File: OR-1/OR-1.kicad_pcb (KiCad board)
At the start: 2 copper layers, 23 x 39.7 mm, 7 parts

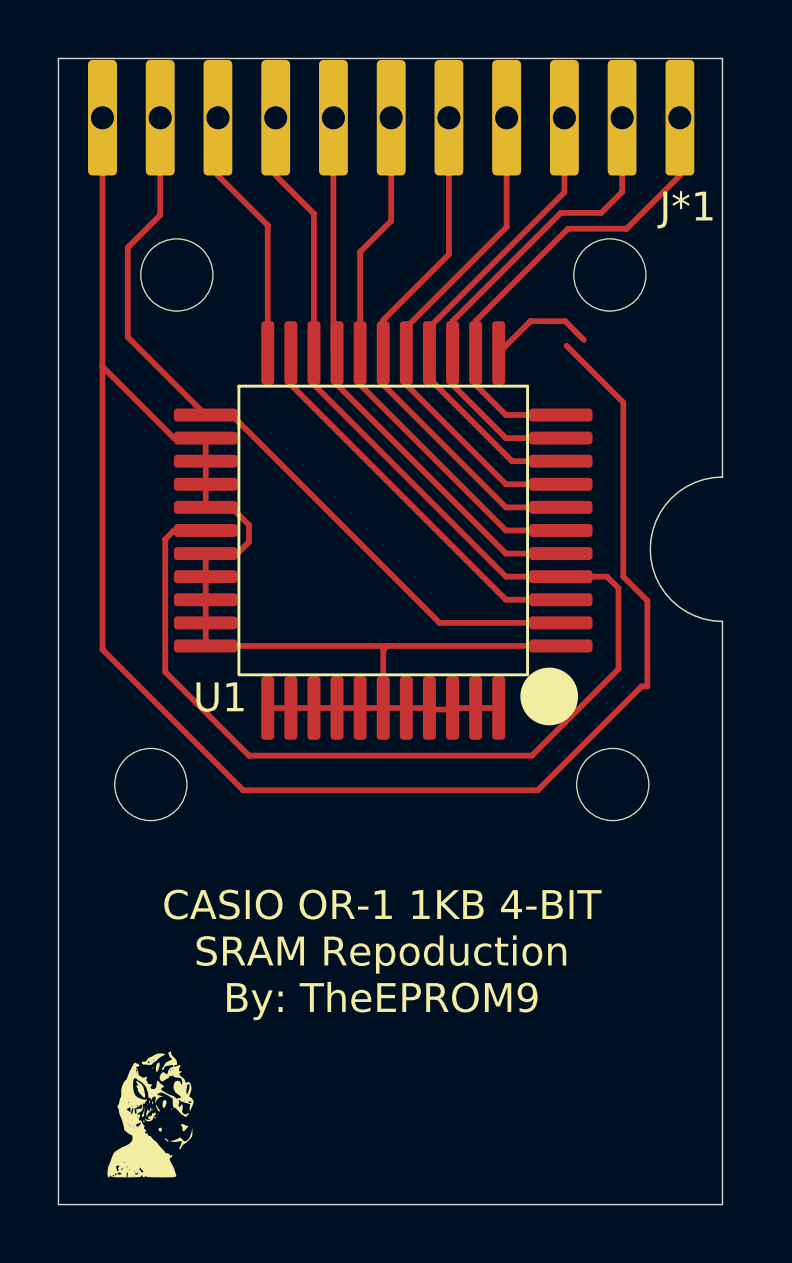
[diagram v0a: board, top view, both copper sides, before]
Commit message: Updated Hole Spacing
Bottom holes were incorrect, ironic really.
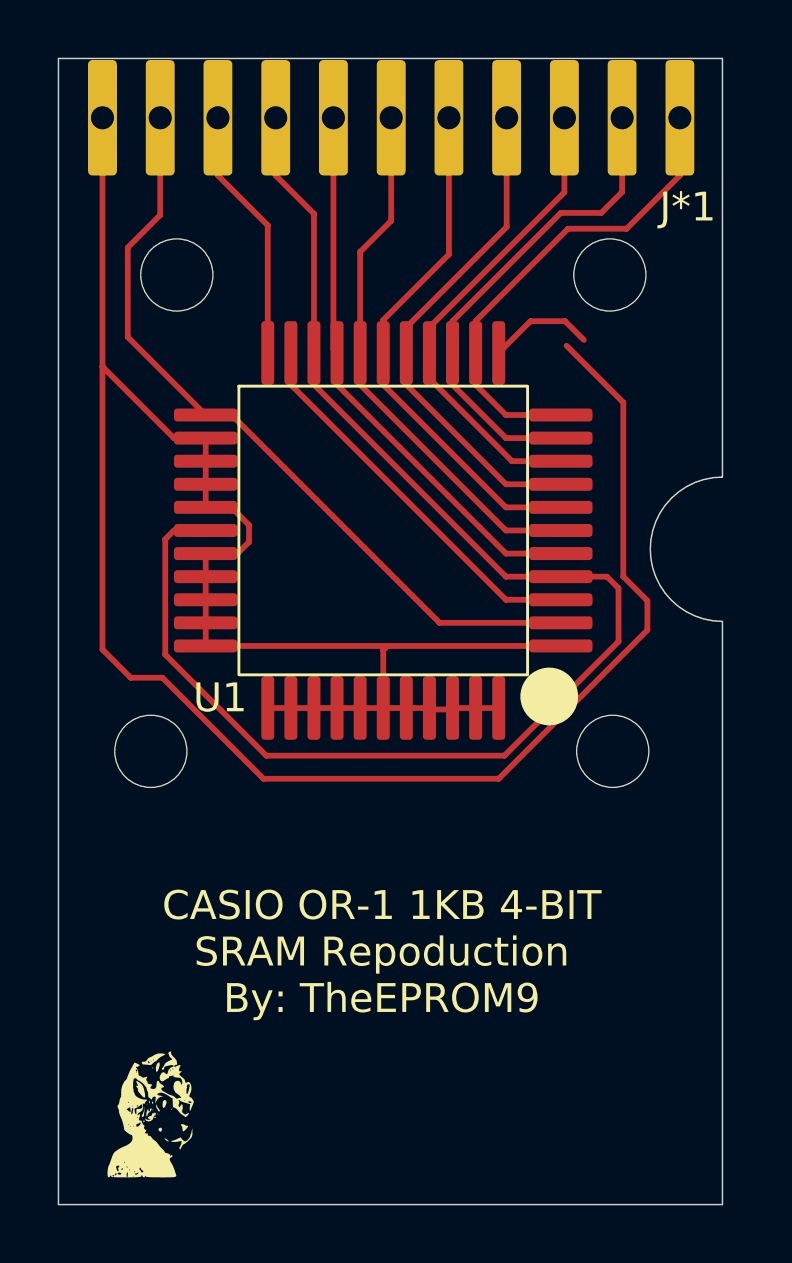
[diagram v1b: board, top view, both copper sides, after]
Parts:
- moved ? 1.15 mm to (141.6, 87.2)
- moved ? 1.15 mm to (157.6, 87.2)
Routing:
- net Net-(J*1-INT/GND): track 89.7 -> 88.2 mm
- net Net-(J*1-VDD2): track 50.3 -> 49.4 mm
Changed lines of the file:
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@@
 	(footprint ""
 		(layer "F.Cu")
-		(at 141.6 88.4)
+		(at 141.6 87.25)
 		(property "Reference" ""
 			(at 0 0 0)
@@
 	(footprint ""
 		(layer "F.Cu")
-		(at 157.6 88.4)
+		(at 157.6 87.25)
 		(property "Reference" ""
 			(at 0 0 0)
@@
 	)
 	(segment
+		(start 142.400001 79.6)
+		(end 142.099 79.901001)
+		(width 0.2)
+		(layer "F.Cu")
+		(net 2)
+	)
+	(segment
 		(start 147.25 74.549999)
 		(end 153.900001 81.2)
@@
 	)
 	(segment
-		(start 142.400001 79.6)
-		(end 142.099 79.901001)
-		(width 0.2)
-		(layer "F.Cu")
-		(net 2)
-	)
-	(segment
-		(start 154.8 87.4)
-		(end 157.8 84.4)
-		(width 0.2)
-		(layer "F.Cu")
-		(net 2)
-	)
-	(segment
-		(start 145 87.4)
-		(end 154.8 87.4)
+		(start 157.8 83.45)
+		(end 157.8 81.6)
 		(width 0.2)
 		(layer "F.Cu")
@@
 	)
 	(segment
+		(start 142.099 79.901001)
+		(end 142.099 83.899)
+		(width 0.2)
+		(layer "F.Cu")
+		(net 2)
+	)
+	(segment
+		(start 153.85 87.4)
+		(end 157.8 83.45)
+		(width 0.2)
+		(layer "F.Cu")
+		(net 2)
+	)
+	(segment
+		(start 145.6 87.4)
+		(end 153.85 87.4)
+		(width 0.2)
+		(layer "F.Cu")
+		(net 2)
+	)
+	(segment
+		(start 142.099 83.899)
+		(end 145.6 87.4)
+		(width 0.2)
+		(layer "F.Cu")
+		(net 2)
+	)
+	(segment
+		(start 147.25 68.629999)
+		(end 147.25 73.45)
+		(width 0.2)
+		(layer "F.Cu")
+		(net 2)
+	)
+	(segment
+		(start 147.25 73.45)
+		(end 147.25 74.549999)
+		(width 0.2)
+		(layer "F.Cu")
+		(net 2)
+	)
+	(segment
+		(start 153.900001 81.2)
+		(end 155.8 81.2)
+		(width 0.2)
+		(layer "F.Cu")
+		(net 2)
+	)
+	(segment
 		(start 157.4 81.2)
 		(end 155.8 81.2)
@@
 	)
 	(segment
-		(start 142.099 84.499)
-		(end 145 87.4)
-		(width 0.2)
-		(layer "F.Cu")
-		(net 2)
-	)
-	(segment
 		(start 143.5 79.6)
 		(end 142.400001 79.6)
@@
 	)
 	(segment
-		(start 142.099 79.901001)
-		(end 142.099 84.499)
-		(width 0.2)
-		(layer "F.Cu")
-		(net 2)
-	)
-	(segment
-		(start 157.8 84.4)
-		(end 157.8 81.6)
-		(width 0.2)
-		(layer "F.Cu")
-		(net 2)
-	)
-	(segment
-		(start 147.25 68.629999)
-		(end 147.25 73.45)
-		(width 0.2)
-		(layer "F.Cu")
-		(net 2)
-	)
-	(segment
-		(start 147.25 73.45)
-		(end 147.25 74.549999)
-		(width 0.2)
-		(layer "F.Cu")
-		(net 2)
-	)
-	(segment
-		(start 153.900001 81.2)
-		(end 155.8 81.2)
-		(width 0.2)
-		(layer "F.Cu")
-		(net 2)
-	)
-	(segment
 		(start 153.900001 82)
 		(end 155.8 82)
@@
 	)
 	(segment
+		(start 140.9 84.7)
+		(end 139.925 83.725)
+		(width 0.2)
+		(layer "F.Cu")
+		(net 9)
+	)
+	(segment
 		(start 157.9661 75.1661)
 		(end 156 73.2)
@@
 	)
 	(segment
+		(start 158.8 82.0329)
+		(end 158.8 83.05)
+		(width 0.2)
+		(layer "F.Cu")
+		(net 9)
+	)
+	(segment
 		(start 143.5 80.4)
 		(end 143.5 83.6)
@@
 	)
 	(segment
-		(start 158.8 85)
-		(end 158.8 82.0329)
+		(start 158.8 83.05)
+		(end 153.65 88.2)
+		(width 0.2)
+		(layer "F.Cu")
+		(net 9)
+	)
+	(segment
+		(start 142 84.7)
+		(end 140.9 84.7)
 		(width 0.2)
 		(layer "F.Cu")
@@
 	)
 	(segment
+		(start 145.5 88.2)
+		(end 142 84.7)
+		(width 0.2)
+		(layer "F.Cu")
+		(net 9)
+	)
+	(segment
 		(start 145 79.999999)
 		(end 144.599999 80.4)
@@
 	)
 	(segment
-		(start 158.6 85)
-		(end 158.8 85)
-		(width 0.2)
-		(layer "F.Cu")
-		(net 9)
-	)
-	(segment
-		(start 139.925 83.725)
-		(end 144.8 88.6)
-		(width 0.2)
-		(layer "F.Cu")
-		(net 9)
-	)
-	(segment
 		(start 143.5 83.6)
 		(end 149.8 83.6)
@@
 	)
 	(segment
-		(start 144.8 88.6)
-		(end 155 88.6)
-		(width 0.2)
-		(layer "F.Cu")
-		(net 9)
-	)
-	(segment
 		(start 144.599999 80.4)
 		(end 143.5 80.4)
@@
 	)
 	(segment
-		(start 155 88.6)
-		(end 158.6 85)
-		(width 0.2)
-		(layer "F.Cu")
+		(start 153.65 88.2)
+		(end 145.5 88.2)
+		(width 0.2)
+		(layer "F.Cu")
